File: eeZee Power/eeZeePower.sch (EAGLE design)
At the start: 11 parts

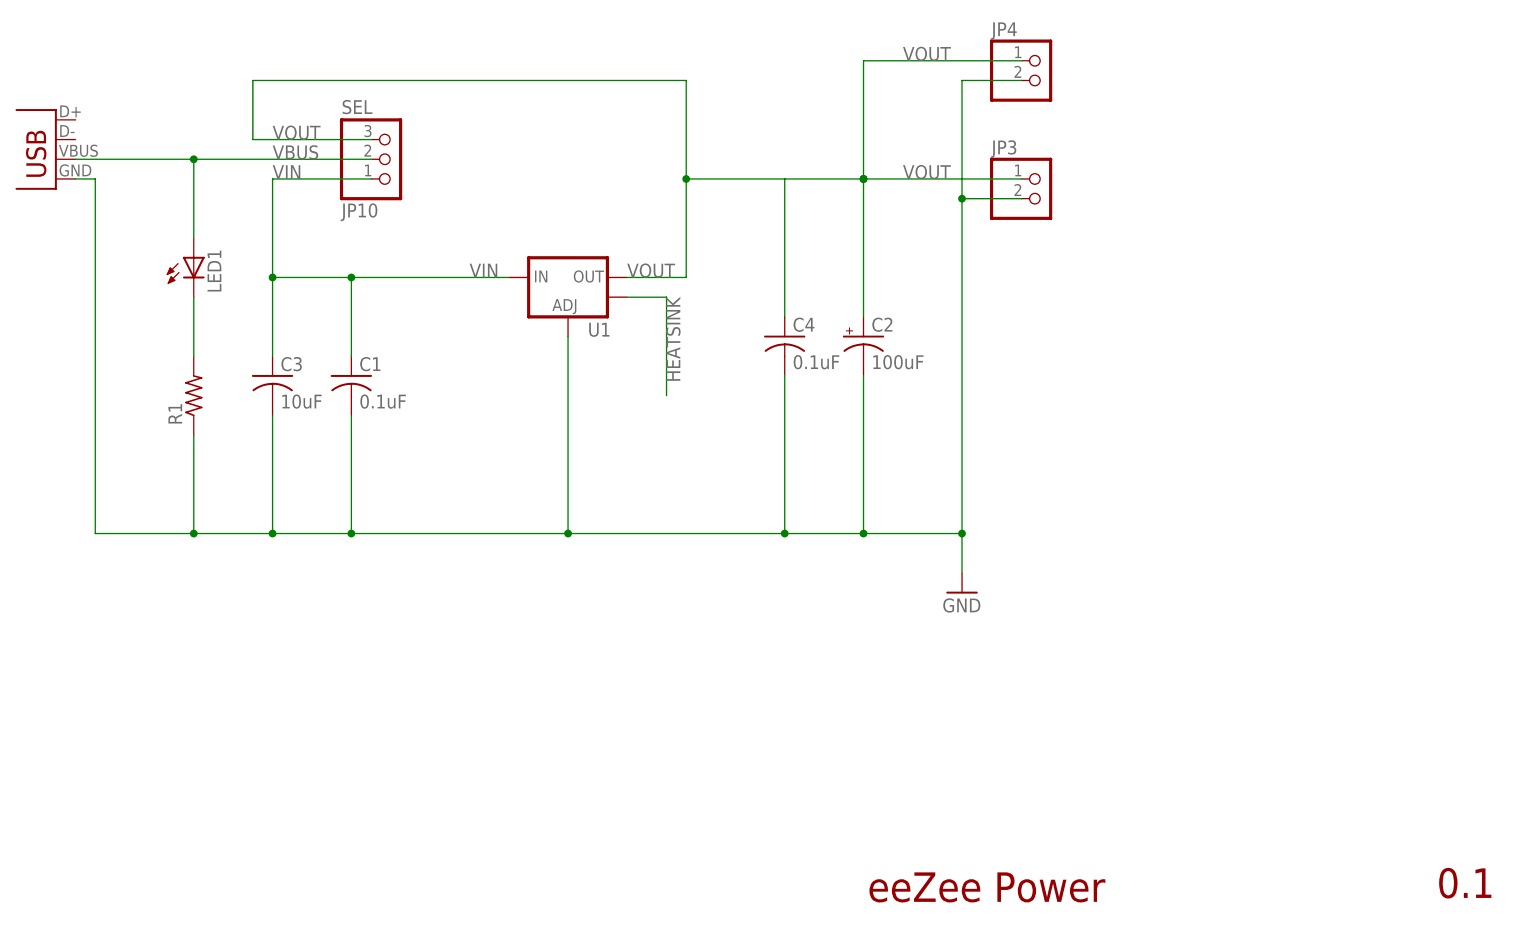
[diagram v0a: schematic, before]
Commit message: Fixed jumper labels
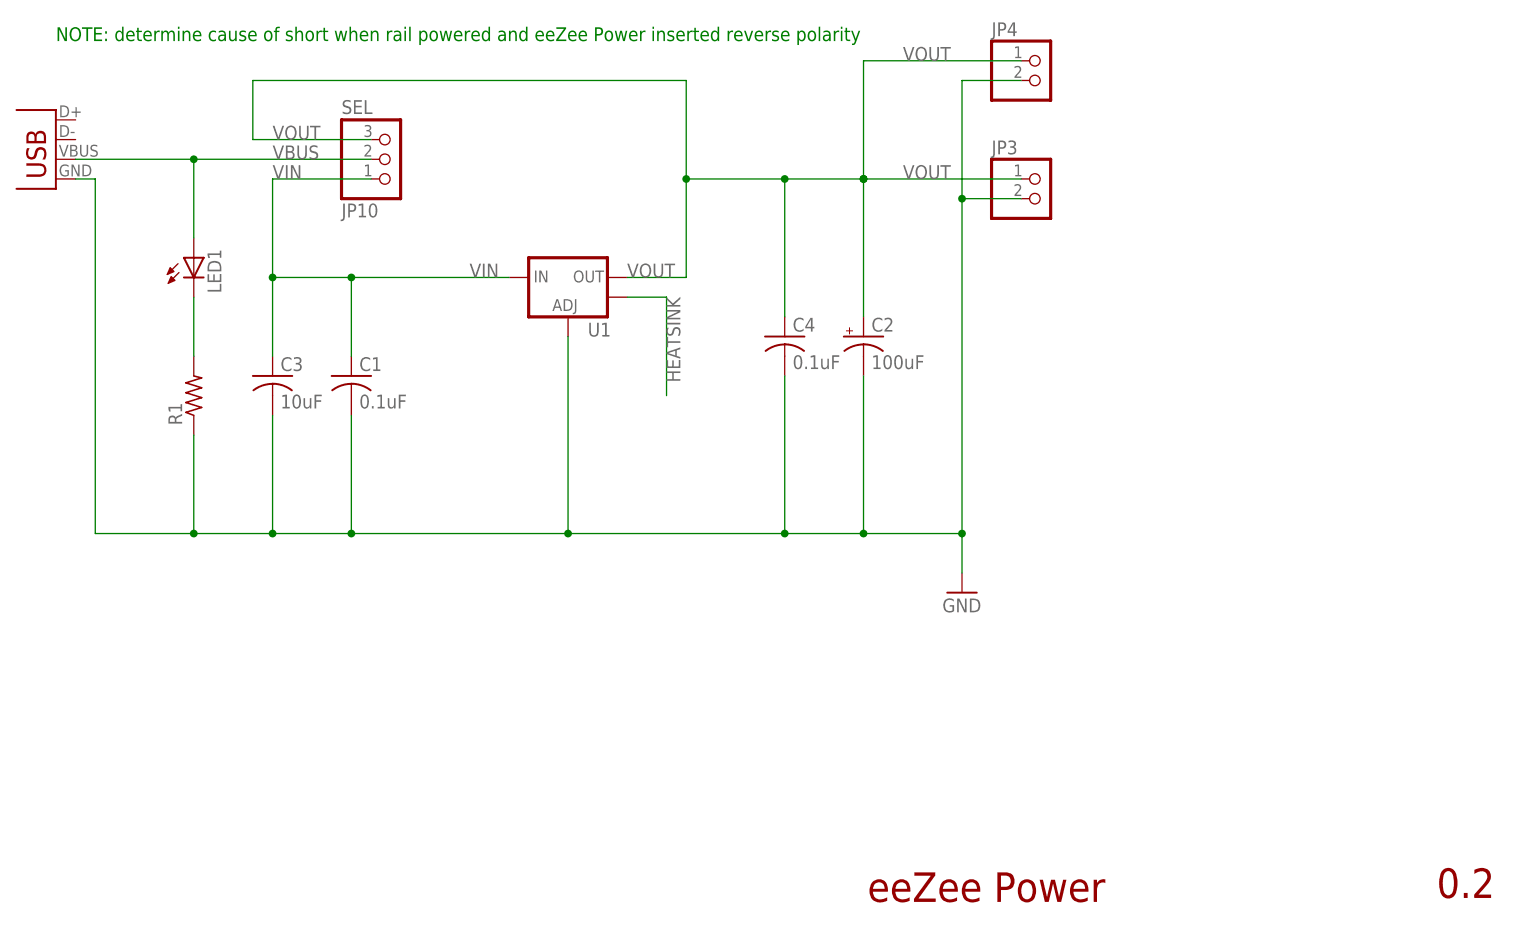
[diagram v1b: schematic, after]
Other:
- note added: "0.2"
- note added: "NOTE: determine cause of short when rail powered and eeZee Power inserted reverse polarity"
- note removed: "0.1"
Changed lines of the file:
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@@
 <grid distance="0.1" unitdist="inch" unit="inch" style="lines" multiple="1" display="no" altdistance="0.01" altunitdist="inch" altunit="inch"/>
 <layers>
-<layer number="1" name="Top" color="4" fill="1" visible="yes" active="no"/>
-<layer number="16" name="Bottom" color="1" fill="1" visible="yes" active="no"/>
-<layer number="17" name="Pads" color="2" fill="1" visible="yes" active="no"/>
-<layer number="18" name="Vias" color="2" fill="1" visible="yes" active="no"/>
-<layer number="19" name="Unrouted" color="6" fill="1" visible="yes" active="no"/>
-<layer number="20" name="Dimension" color="15" fill="1" visible="yes" active="no"/>
-<layer number="21" name="tPlace" color="7" fill="1" visible="yes" active="no"/>
-<layer number="22" name="bPlace" color="7" fill="1" visible="yes" active="no"/>
-<layer number="23" name="tOrigins" color="15" fill="1" visible="yes" active="no"/>
-<layer number="24" name="bOrigins" color="15" fill="1" visible="yes" active="no"/>
-<layer number="25" name="tNames" color="7" fill="1" visible="yes" active="no"/>
-<layer number="26" name="bNames" color="7" fill="1" visible="yes" active="no"/>
-<layer number="27" name="tValues" color="7" fill="1" visible="yes" active="no"/>
-<layer number="28" name="bValues" color="7" fill="1" visible="yes" active="no"/>
+<layer number="1" name="Top" color="4" fill="1" visible="no" active="no"/>
+<layer number="16" name="Bottom" color="1" fill="1" visible="no" active="no"/>
+<layer number="17" name="Pads" color="2" fill="1" visible="no" active="no"/>
+<layer number="18" name="Vias" color="2" fill="1" visible="no" active="no"/>
+<layer number="19" name="Unrouted" color="6" fill="1" visible="no" active="no"/>
+<layer number="20" name="Dimension" color="15" fill="1" visible="no" active="no"/>
+<layer number="21" name="tPlace" color="7" fill="1" visible="no" active="no"/>
+<layer number="22" name="bPlace" color="7" fill="1" visible="no" active="no"/>
+<layer number="23" name="tOrigins" color="15" fill="1" visible="no" active="no"/>
+<layer number="24" name="bOrigins" color="15" fill="1" visible="no" active="no"/>
+<layer number="25" name="tNames" color="7" fill="1" visible="no" active="no"/>
+<layer number="26" name="bNames" color="7" fill="1" visible="no" active="no"/>
+<layer number="27" name="tValues" color="7" fill="1" visible="no" active="no"/>
+<layer number="28" name="bValues" color="7" fill="1" visible="no" active="no"/>
 <layer number="29" name="tStop" color="7" fill="3" visible="no" active="no"/>
 <layer number="30" name="bStop" color="7" fill="6" visible="no" active="no"/>
@@
 <layer number="35" name="tGlue" color="7" fill="4" visible="no" active="no"/>
 <layer number="36" name="bGlue" color="7" fill="5" visible="no" active="no"/>
-<layer number="37" name="tTest" color="7" fill="1" visible="yes" active="no"/>
-<layer number="38" name="bTest" color="7" fill="1" visible="yes" active="no"/>
+<layer number="37" name="tTest" color="7" fill="1" visible="no" active="no"/>
+<layer number="38" name="bTest" color="7" fill="1" visible="no" active="no"/>
 <layer number="39" name="tKeepout" color="4" fill="11" visible="no" active="no"/>
 <layer number="40" name="bKeepout" color="1" fill="11" visible="no" active="no"/>
@@
 <layer number="44" name="Drills" color="7" fill="1" visible="no" active="no"/>
 <layer number="45" name="Holes" color="7" fill="1" visible="no" active="no"/>
-<layer number="46" name="Milling" color="3" fill="1" visible="yes" active="no"/>
-<layer number="47" name="Measures" color="7" fill="1" visible="yes" active="no"/>
-<layer number="48" name="Document" color="7" fill="1" visible="yes" active="no"/>
-<layer number="49" name="Reference" color="7" fill="1" visible="yes" active="no"/>
-<layer number="50" name="dxf" color="7" fill="1" visible="yes" active="no"/>
-<layer number="51" name="tDocu" color="7" fill="1" visible="yes" active="no"/>
-<layer number="52" name="bDocu" color="7" fill="1" visible="yes" active="no"/>
-<layer number="53" name="tGND_GNDA" color="7" fill="9" visible="yes" active="no"/>
-<layer number="54" name="bGND_GNDA" color="1" fill="9" visible="yes" active="no"/>
-<layer number="56" name="wert" color="7" fill="1" visible="yes" active="no"/>
+<layer number="46" name="Milling" color="3" fill="1" visible="no" active="no"/>
+<layer number="47" name="Measures" color="7" fill="1" visible="no" active="no"/>
+<layer number="48" name="Document" color="7" fill="1" visible="no" active="no"/>
+<layer number="49" name="Reference" color="7" fill="1" visible="no" active="no"/>
+<layer number="50" name="dxf" color="7" fill="1" visible="no" active="no"/>
+<layer number="51" name="tDocu" color="7" fill="1" visible="no" active="no"/>
+<layer number="52" name="bDocu" color="7" fill="1" visible="no" active="no"/>
+<layer number="53" name="tGND_GNDA" color="7" fill="9" visible="no" active="no"/>
+<layer number="54" name="bGND_GNDA" color="1" fill="9" visible="no" active="no"/>
+<layer number="56" name="wert" color="7" fill="1" visible="no" active="no"/>
 <layer number="91" name="Nets" color="2" fill="1" visible="yes" active="yes"/>
 <layer number="92" name="Busses" color="1" fill="1" visible="yes" active="yes"/>
@@
 <plain>
 <text x="160.528" y="23.622" size="3.81" layer="94">eeZee Power</text>
-<text x="233.934" y="24.13" size="3.81" layer="94">0.1</text>
+<text x="233.934" y="24.13" size="3.81" layer="94">0.2</text>
+<text x="55.88" y="134.62" size="1.778" layer="91">NOTE: determine cause of short when rail powered and eeZee Power inserted reverse polarity</text>
 </plain>
 <instances>
@@
 <label x="129.54" y="104.14" size="1.778" layer="95"/>
 <label x="165.1" y="116.84" size="1.778" layer="95"/>
-</segment>
-</net>
+<junction x="149.86" y="116.84"/>
+</segment>
+</net>
